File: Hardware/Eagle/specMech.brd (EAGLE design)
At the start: 142.2 x 121.9 mm, 78 parts, among them J1 PINHD-1X8-MOLEX-SHROUD, J3 PINHD-1X8-MOLEX-SHROUD, J4 PINHD-1X8-MOLEX-SHROUD, J5 XPORT, J6 Molex 0022232081, J8 Molex 0022232081, U1 MCP23008-E/SO, U10 ADS1115, U11 MCP23008-E/SO, U12 74HC2G17TSSOP-6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

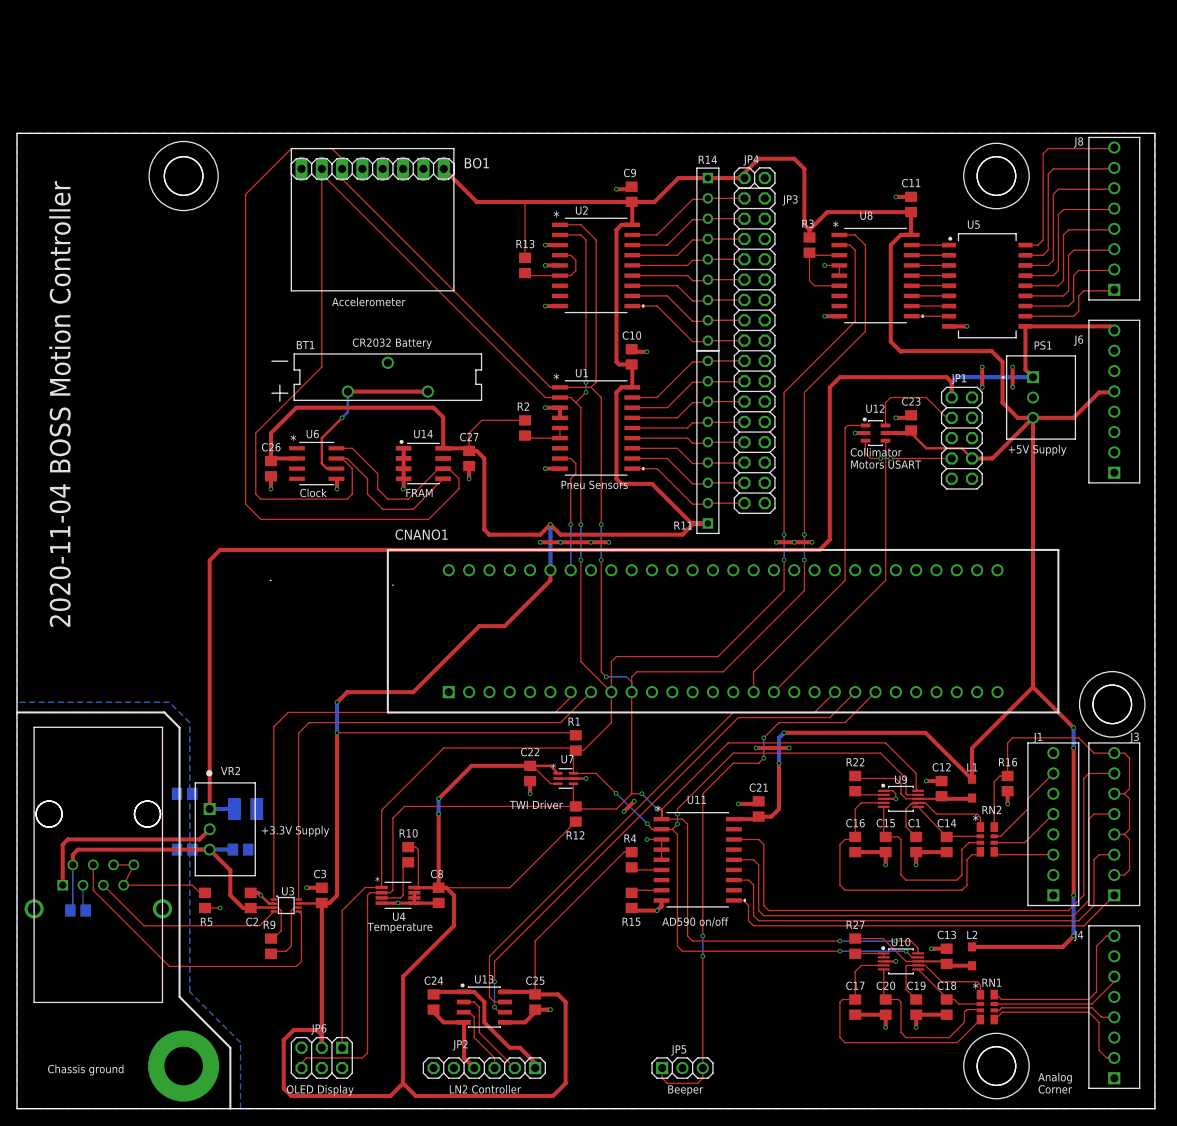
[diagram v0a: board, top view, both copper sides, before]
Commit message: Used later version of XPORT-2
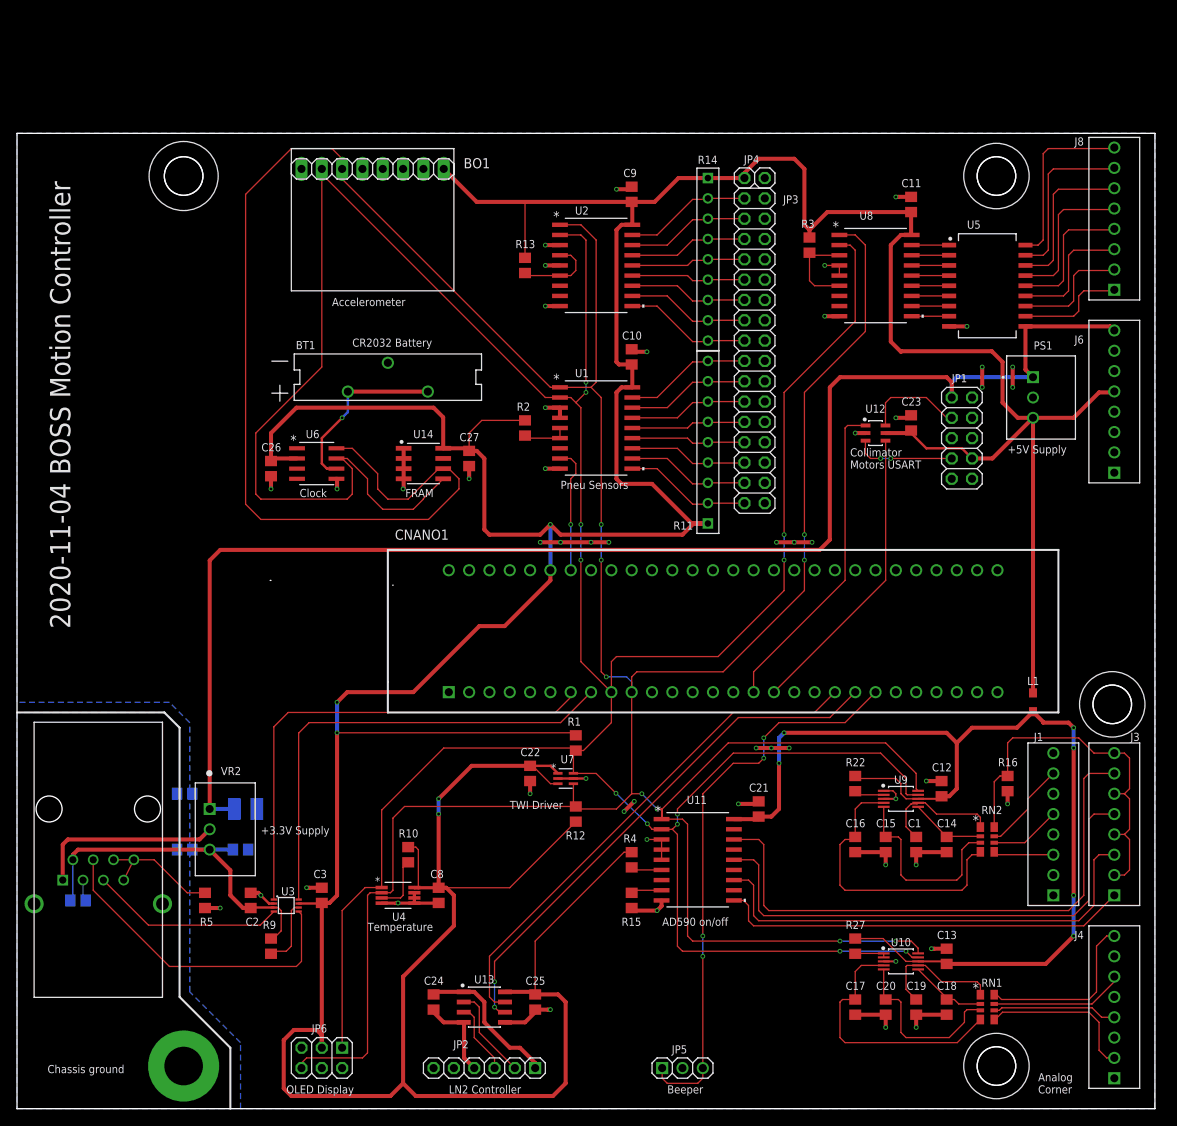
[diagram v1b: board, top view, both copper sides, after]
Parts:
- removed J5: XPORT, AUmlib:XPORT-2
- removed L2: MMZ2012Y152BT000, AUmlib:INDC2012X87N
- added J7: (no value), AUmlib:XPORT-2
- moved L1 13.2 mm to (127.0, 50.8)
- moved R8 1.27 mm to (7.62, 26.0)
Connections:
- removed net N$6: C13.1, L2.1, R27.1, U10.8
- removed net N$7: C12.1, L1.1, R22.1, U9.8
- new net FILT5V: C12.1, C13.1, C21.1, L1.1, R22.1, R27.1, U10.8, U11.18, U9.8
- net +3.3V: now also J7.3.3V; no longer J5.3.3V
- net +5V: no longer C21.1, L2.2, U11.18
- net CP3: now also J7.CP1, J7.CP2, J7.CP3; no longer J5.CP1, J5.CP2, J5.CP3
- net GND: now also J7.GND; no longer J5.GND
- net GND-1: now also J7.P$1, J7.P$2; no longer J5.P$1, J5.P$2
- net XP-RX: now also J7.RX; no longer J5.RX
- net XP-TX: now also J7.TX; no longer J5.TX
- net XP/RST: now also J7./RST; no longer J5./RST
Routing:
- net FILT5V: track 0.00 -> 132.5 mm, vias 0 -> 6
- net +5V: track 734.8 -> 632.3 mm, vias 11 -> 5
- net N$7: track 16.9 -> 0.00 mm
- net N$6: track 16.0 -> 0.00 mm
- net +3.3V: track 47.7 -> 46.5 mm
- net XP/RST: track 3.31 -> 2.67 mm
- net XP-TX: track 39.8 -> 40.4 mm
- net GND: track 156.2 -> 155.6 mm, vias 51 -> 52
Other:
- outline, holes or cut-outs redrawn

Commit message: Updated board label
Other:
- board text added: "2020-11-06 BOSS Motion Controller"
- board text removed: "2020-11-04 BOSS Motion Controller"
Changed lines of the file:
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@@
 </layers>
 <board>
-<fusionsync huburn="a.cGVyc29uYWw6dWUyZDgyNjcx" projecturn="a.cGVyc29uYWw6dWUyZDgyNjcxIzIwMTgxMjIwMTY2NDc1MjMx" f3durn="urn:adsk.wipprod:dm.lineage:JfX9Sz9hQ7uElenyZAoR3A" pcbguid="" lastpulledtime="" lastsyncedchangeguid="" latestrevisionid="edd4713a-48d5-424f-a670-f3ae8c65c417" lastsyncedrevisionid="edd4713a-48d5-424f-a670-f3ae8c65c417" lastboardhashguid="fffc4151-e3b3-b3b8-f1e6-e82c56d8d4b8" lastpushedtime="2020-11-06T00:58:21Z" linktopcb3d="true"/>
+<fusionsync huburn="a.cGVyc29uYWw6dWUyZDgyNjcx" projecturn="a.cGVyc29uYWw6dWUyZDgyNjcxIzIwMTgxMjIwMTY2NDc1MjMx" f3durn="urn:adsk.wipprod:dm.lineage:JfX9Sz9hQ7uElenyZAoR3A" pcbguid="" lastpulledtime="" lastsyncedchangeguid="" latestrevisionid="eacfc655-f4ba-4c96-9010-6dfc90ade349" lastsyncedrevisionid="eacfc655-f4ba-4c96-9010-6dfc90ade349" lastboardhashguid="e8502fe8-18c8-dd34-cef3-7213a076c4e5" lastpushedtime="2020-11-06T17:49:10Z" linktopcb3d="true"/>
 <plain>
 <circle x="122.428" y="116.586" radius="4.0894" width="0.1524" layer="21"/>
@@
 <text x="127.635" y="1.905" size="1.016" layer="21" font="vector">Analog
 Corner</text>
-<text x="6.6675" y="60.0075" size="2.54" layer="21" rot="R90">2020-11-04 BOSS Motion Controller</text>
+<text x="12.065" y="58.1025" size="2.54" layer="21" rot="R90">2020-11-06 BOSS Motion Controller</text>
 <wire x1="0" y1="49.53" x2="18.415" y2="49.53" width="0.254" layer="21"/>
 <wire x1="18.415" y1="49.53" x2="20.32" y2="47.625" width="0.254" layer="21"/>
@@
 <wire x1="92.3925" y1="45.085" x2="94.2975" y2="45.085" width="0.508" layer="1"/>
 <wire x1="94.2975" y1="45.085" x2="96.52" y2="45.085" width="0.508" layer="1"/>
-<wire x1="137.16" y1="84.582" x2="137.16" y2="92.202" width="0" layer="19" extent="1-1"/>
-<wire x1="137.16" y1="79.502" x2="137.16" y2="84.582" width="0" layer="19" extent="1-1"/>
-<wire x1="127" y1="88.9" x2="137.16" y2="92.202" width="0" layer="19" extent="1-1"/>
-<wire x1="124.46" y1="90.17" x2="127" y2="88.9" width="0" layer="19" extent="1-1"/>
-<wire x1="120.65" y1="92.71" x2="124.46" y2="92.71" width="0" layer="19" extent="1-1"/>
-<wire x1="118.745" y1="97.79" x2="120.65" y2="92.71" width="0" layer="19" extent="1-1"/>
-<wire x1="116.84" y1="83.82" x2="120.65" y2="90.17" width="0" layer="19" extent="1-1"/>
-<wire x1="116.84" y1="78.74" x2="116.84" y2="83.82" width="0" layer="19" extent="1-1"/>
-<wire x1="111.76" y1="86.675" x2="116.84" y2="83.82" width="0" layer="19" extent="1-1"/>
-<wire x1="106.0708" y1="84.455" x2="109.855" y2="86.36" width="0" layer="19" extent="1-1"/>
-<wire x1="93.472" y1="83.312" x2="104.775" y2="84.455" width="0" layer="19" extent="1-1"/>
-<wire x1="93.472" y1="85.852" x2="93.472" y2="83.312" width="0" layer="19" extent="1-1"/>
-<wire x1="93.472" y1="88.392" x2="93.472" y2="85.852" width="0" layer="19" extent="1-1"/>
-<wire x1="93.472" y1="90.932" x2="93.472" y2="88.392" width="0" layer="19" extent="1-1"/>
-<wire x1="93.472" y1="93.472" x2="93.472" y2="90.932" width="0" layer="19" extent="1-1"/>
-<wire x1="93.472" y1="96.012" x2="93.472" y2="93.472" width="0" layer="19" extent="1-1"/>
-<wire x1="93.472" y1="98.552" x2="93.472" y2="96.012" width="0" layer="19" extent="1-1"/>
-<wire x1="93.472" y1="101.092" x2="93.472" y2="98.552" width="0" layer="19" extent="1-1"/>
-<wire x1="93.472" y1="103.632" x2="93.472" y2="101.092" width="0" layer="19" extent="1-1"/>
-<wire x1="93.472" y1="106.172" x2="93.472" y2="103.632" width="0" layer="19" extent="1-1"/>
-<wire x1="93.472" y1="108.712" x2="93.472" y2="106.172" width="0" layer="19" extent="1-1"/>
-<wire x1="93.472" y1="111.252" x2="93.472" y2="108.712" width="0" layer="19" extent="1-1"/>
-<wire x1="93.472" y1="113.792" x2="93.472" y2="111.252" width="0" layer="19" extent="1-1"/>
-<wire x1="93.472" y1="116.332" x2="93.472" y2="113.792" width="0" layer="19" extent="1-1"/>
-<wire x1="93.472" y1="80.772" x2="93.472" y2="83.312" width="0" layer="19" extent="1-1"/>
-<wire x1="93.472" y1="78.232" x2="93.472" y2="80.772" width="0" layer="19" extent="1-1"/>
-<wire x1="93.472" y1="75.692" x2="93.472" y2="78.232" width="0" layer="19" extent="1-1"/>
-<wire x1="94.9325" y1="70.8025" x2="93.472" y2="75.692" width="0" layer="19" extent="1-1"/>
-<wire x1="89.535" y1="67.31" x2="94.9325" y2="70.8025" width="0" layer="19" extent="1-1"/>
-<wire x1="100.965" y1="99.06" x2="93.472" y2="98.552" width="0" layer="19" extent="1-1"/>
-<wire x1="102.7938" y1="104.14" x2="102.7938" y2="99.06" width="0" layer="19" extent="1-1"/>
-<wire x1="109.855" y1="113.9698" x2="102.7938" y2="105.41" width="0" layer="19" extent="1-1"/>
-<wire x1="112.395" y1="67.31" x2="116.84" y2="78.74" width="0" layer="19" extent="1-1"/>
-<wire x1="78.74" y1="94.615" x2="93.472" y2="93.472" width="0" layer="19" extent="1-1"/>
-<wire x1="67.8688" y1="100.33" x2="76.835" y2="94.93" width="0" layer="19" extent="1-1"/>
-<wire x1="67.8688" y1="105.41" x2="67.8688" y2="100.33" width="0" layer="19" extent="1-1"/>
-<wire x1="67.8688" y1="107.95" x2="67.8688" y2="105.41" width="0" layer="19" extent="1-1"/>
-<wire x1="74.93" y1="114.935" x2="67.8688" y2="107.95" width="0" layer="19" extent="1-1"/>
-<wire x1="67.8688" y1="87.63" x2="76.835" y2="94.93" width="0" layer="19" extent="1-1"/>
-<wire x1="67.8688" y1="80.01" x2="67.8688" y2="86.36" width="0" layer="19" extent="1-1"/>
-<wire x1="67.945" y1="70.8025" x2="67.8688" y2="80.01" width="0" layer="19" extent="1-1"/>
-<wire x1="64.135" y1="67.31" x2="65.405" y2="70.8025" width="0" layer="19" extent="1-1"/>
-<wire x1="56.515" y1="80.33" x2="66.04" y2="80.01" width="0" layer="19" extent="1-1"/>
-<wire x1="48.3266" y1="78.74" x2="56.515" y2="78.74" width="0" layer="19" extent="1-1"/>
-<wire x1="40.005" y1="77.47" x2="48.26" y2="77.47" width="0" layer="19" extent="1-1"/>
-<wire x1="31.75" y1="79.06" x2="39.9288" y2="78.74" width="0" layer="19" extent="1-1"/>
-<wire x1="46.355" y1="93.24" x2="48.3266" y2="82.55" width="0" layer="19" extent="1-1"/>
-<wire x1="112.395" y1="52.07" x2="112.395" y2="67.31" width="0" layer="19" extent="1-1"/>
-<wire x1="113.665" y1="40.9575" x2="112.395" y2="52.07" width="0" layer="19" extent="1-1"/>
-<wire x1="109.855" y1="38.735" x2="113.665" y2="40.9575" width="0" layer="19" extent="1-1"/>
-<wire x1="108.585" y1="32.07" x2="108.3404" y2="38.735" width="0" layer="19" extent="1-1"/>
-<wire x1="112.395" y1="30.48" x2="108.585" y2="30.48" width="0" layer="19" extent="1-1"/>
-<wire x1="123.825" y1="39.69" x2="115.57" y2="40.955" width="0" layer="19" extent="1-1"/>
-<wire x1="129.54" y1="39.37" x2="123.825" y2="39.69" width="0" layer="19" extent="1-1"/>
-<wire x1="129.54" y1="44.45" x2="129.54" y2="39.37" width="0" layer="19" extent="1-1"/>
-<wire x1="129.54" y1="34.29" x2="129.54" y2="39.37" width="0" layer="19" extent="1-1"/>
-<wire x1="129.54" y1="26.67" x2="129.54" y2="34.29" width="0" layer="19" extent="1-1"/>
-<wire x1="114.3" y1="20.0025" x2="112.395" y2="30.48" width="0" layer="19" extent="1-1"/>
-<wire x1="109.855" y1="18.415" x2="114.3" y2="20.0025" width="0" layer="19" extent="1-1"/>
-<wire x1="108.585" y1="11.75" x2="108.3404" y2="18.415" width="0" layer="19" extent="1-1"/>
-<wire x1="112.395" y1="11.75" x2="108.585" y2="11.75" width="0" layer="19" extent="1-1"/>
-<wire x1="137.16" y1="19.05" x2="129.54" y2="26.67" width="0" layer="19" extent="1-1"/>
-<wire x1="137.16" y1="13.97" x2="137.16" y2="19.05" width="0" layer="19" extent="1-1"/>
-<wire x1="137.16" y1="8.89" x2="137.16" y2="13.97" width="0" layer="19" extent="1-1"/>
-<wire x1="137.16" y1="3.81" x2="137.16" y2="8.89" width="0" layer="19" extent="1-1"/>
-<wire x1="96.52" y1="45.085" x2="108.3404" y2="39.735" width="0" layer="19" extent="1-1"/>
-<wire x1="92.71" y1="38.415" x2="92.3925" y2="45.085" width="0" layer="19" extent="1-1"/>
-<wire x1="89.535" y1="52.07" x2="92.3925" y2="45.085" width="0" layer="19" extent="1-1"/>
-<wire x1="80.5688" y1="33.655" x2="90.17" y2="38.1" width="0" layer="19" extent="1-1"/>
-<wire x1="75.8825" y1="37.1475" x2="78.74" y2="33.655" width="0" layer="19" extent="1-1"/>
-<wire x1="80.5688" y1="26.035" x2="80.5688" y2="31.115" width="0" layer="19" extent="1-1"/>
-<wire x1="71.12" y1="41.275" x2="75.8825" y2="37.1475" width="0" layer="19" extent="1-1"/>
-<wire x1="64.135" y1="40.96" x2="67.61" y2="41.275" width="0" layer="19" extent="1-1"/>
-<wire x1="66.675" y1="12.3825" x2="76.835" y2="25.085" width="0" layer="19" extent="1-1"/>
-<wire x1="52.705" y1="25.72" x2="60.9975" y2="10.795" width="0" layer="19" extent="1-1"/>
-<wire x1="38.1" y1="27.62" x2="45.5803" y2="25.695" width="0" layer="19" extent="1-1"/>
-<wire x1="32.105" y1="25.65" x2="36.195" y2="27.6225" width="0" layer="19" extent="1-1"/>
-<wire x1="25.4" y1="25.0825" x2="29.21" y2="26.985" width="0" layer="19" extent="1-1"/>
-<wire x1="28.89" y1="32.385" x2="29.21" y2="26.985" width="0" layer="19" extent="1-16"/>
-<wire x1="29.975" y1="37.465" x2="28.89" y2="32.385" width="0" layer="19" extent="16-16"/>
-<wire x1="24.085" y1="34.925" x2="28.89" y2="32.385" width="0" layer="19" extent="16-16"/>
-<wire x1="21.905" y1="39.37" x2="24.085" y2="34.925" width="0" layer="19" extent="16-16"/>
-<wire x1="50.8" y1="117.475" x2="66.04" y2="107.95" width="0" layer="19" extent="1-1"/>
-<wire x1="83.185" y1="5.08" x2="66.675" y2="12.3825" width="0" layer="19" extent="1-1"/>
-<wire x1="35.56" y1="7.62" x2="32.105" y2="25.65" width="0" layer="19" extent="1-1"/>
-<wire x1="40.64" y1="5.08" x2="35.56" y2="7.62" width="0" layer="19" extent="1-1"/>
 </signal>
 <signal name="+5V">

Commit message: Connected VOFF to GND
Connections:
- net GND: now also CNANO1.VOFF
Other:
- outline, holes or cut-outs redrawn
- board text added: "2020-11-07 BOSS Motion Controller"
- board text removed: "2020-11-06 BOSS Motion Controller"
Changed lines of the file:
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@@
 <text x="127.635" y="1.905" size="1.016" layer="21" font="vector">Analog
 Corner</text>
-<text x="12.065" y="58.1025" size="2.54" layer="21" rot="R90">2020-11-06 BOSS Motion Controller</text>
+<text x="12.065" y="58.1025" size="2.54" layer="21" rot="R90">2020-11-07 BOSS Motion Controller</text>
 <wire x1="0" y1="49.53" x2="18.415" y2="49.53" width="0.254" layer="21"/>
 <wire x1="18.415" y1="49.53" x2="20.32" y2="47.625" width="0.254" layer="21"/>
@@
 <hole x="20.828" y="116.586" drill="4.826"/>
 <circle x="122.428" y="5.334" radius="2.413" width="0" layer="20"/>
-<wire x1="31.6393" y1="66.0352" x2="31.75" y2="66.04" width="0" layer="20"/>
-<wire x1="46.9876" y1="65.4603" x2="46.99" y2="65.405" width="0" layer="20"/>
 <wire x1="46.4103" y1="53.3424" x2="46.355" y2="53.34" width="0" layer="20"/>
 <circle x="20.828" y="116.586" radius="2.413" width="0" layer="20"/>
@@
 <wire x1="92.3925" y1="45.085" x2="94.2975" y2="45.085" width="0.508" layer="1"/>
 <wire x1="94.2975" y1="45.085" x2="96.52" y2="45.085" width="0.508" layer="1"/>
+<contactref element="CNANO1" pad="VOFF"/>
 </signal>
 <signal name="+5V">

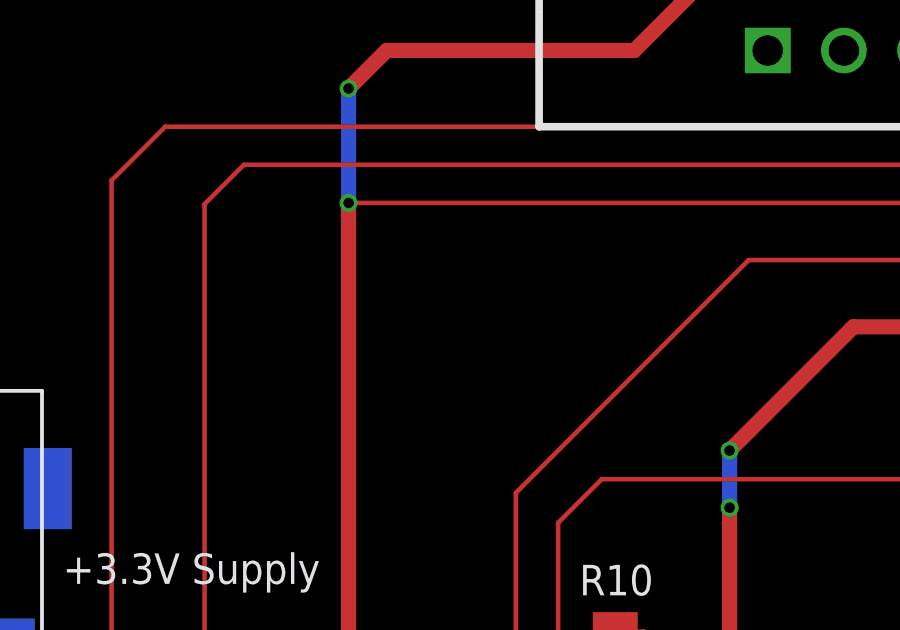
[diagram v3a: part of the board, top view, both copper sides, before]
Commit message: Added +5V power for USB isolator (JST 2-pin header)
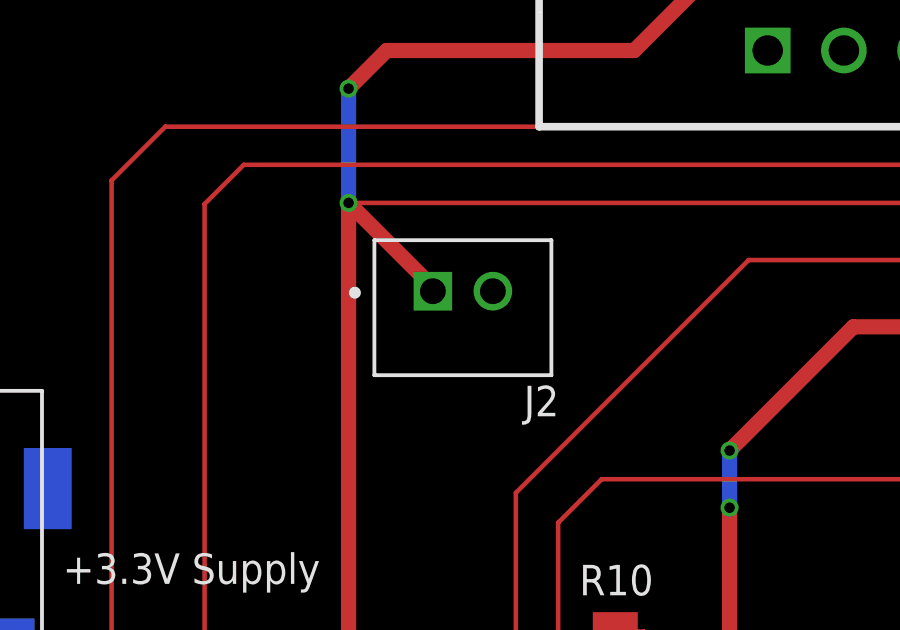
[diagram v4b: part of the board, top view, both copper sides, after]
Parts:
- added J2: JST-2-PIN-2B-PH-K-S(LF)(SN), AUmlib:JST_B2B-PH-K-S(LF)(SN)
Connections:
- net +5V: now also J2.1
- net GND: now also J2.2
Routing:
- net +5V: track 632.3 -> 636.4 mm
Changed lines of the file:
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@@
 </element>
 <element name="J7" library="AUmlib" library_urn="urn:adsk.eagle:library:9166017" package="XPORT-2" package3d_urn="urn:adsk.eagle:package:18328251/5" value="" x="10.16" y="31.115" smashed="yes" rot="R270"/>
+<element name="J2" library="AUmlib" library_urn="urn:adsk.eagle:library:9166017" package="JST_B2B-PH-K-S(LF)(SN)" package3d_urn="urn:adsk.eagle:package:24616272/2" value="JST-2-PIN-2B-PH-K-S(LF)(SN)" x="43.815" y="43.4975" smashed="yes" rot="R180">
+<attribute name="DESCRIPTION" value=" Connector Header Through Hole 2 position 0.079 (2.00mm) " x="43.815" y="43.4975" size="1.778" layer="27" rot="R180" display="off"/>
+<attribute name="DIGI-KEY_PART_NUMBER" value="455-1704-ND" x="43.815" y="43.4975" size="1.778" layer="27" rot="R180" display="off"/>
+<attribute name="MF" value="JST Sales" x="43.815" y="43.4975" size="1.778" layer="27" rot="R180" display="off"/>
+<attribute name="MP" value="B2B-PH-K-S(LF)(SN)" x="43.815" y="43.4975" size="1.778" layer="27" rot="R180" display="off"/>
+<attribute name="NAME" x="47.01981875" y="40.89358125" size="1.01753125" layer="25" rot="R180"/>
+<attribute name="PACKAGE" value="None" x="43.815" y="43.4975" size="1.778" layer="27" rot="R180" display="off"/>
+<attribute name="PURCHASE-URL" value="https://pricing.snapeda.com/search/part/B2B-PH-K-S(LF)(SN)/?ref=eda" x="43.815" y="43.4975" size="1.778" layer="27" rot="R180" display="off"/>
+<attribute name="VALUE" x="47.11638125" y="47.099009375" size="1.01643125" layer="27" rot="R180"/>
+</element>
 </elements>
 <signals>
@@
 <wire x1="94.2975" y1="45.085" x2="96.52" y2="45.085" width="0.508" layer="1"/>
 <contactref element="CNANO1" pad="VOFF"/>
+<contactref element="J2" pad="2"/>
 </signal>
 <signal name="+5V">
@@
 <wire x1="60.96" y1="60.325" x2="57.785" y2="60.325" width="0.508" layer="1"/>
 <wire x1="127" y1="86.36" x2="127" y2="51.975" width="0.508" layer="1"/>
+<contactref element="J2" pad="1"/>
+<wire x1="40.005" y1="46.99" x2="42.815" y2="44.18" width="0.508" layer="1"/>
+<wire x1="42.815" y1="44.18" x2="42.815" y2="44.0475" width="0.508" layer="1"/>
 </signal>
 <signal name="XP-TX">
